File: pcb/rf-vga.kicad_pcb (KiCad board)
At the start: 2 copper layers, 47 parts, among them J1 TEST CONNECTOR, J4 SWD Programming Header, Q1 2N7002, Q2 2N7002, Q3 2N7002, Q4 2N7002, U1 HMC625B, U2 LM1117-3.3, U3 ﻿STM32L010C6

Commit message: PCB updates
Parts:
- added C26: 1u, Capacitor_SMD:C_0603_1608Metric, F.Cu at (189.7, 133.3)
- added C27: 1u, Capacitor_SMD:C_0603_1608Metric, F.Cu at (193.8, 133.3)
- added FB1: GZ2012D601TF, Inductor_SMD:L_0805_2012Metric, F.Cu at (255.0, 97.7)
- added FB2: GZ2012D601TF, Inductor_SMD:L_0805_2012Metric, F.Cu at (255.0, 100.5)
- added J2: Input, parts:SMA_Samtec_SMA-J-P-X-ST-EM1_EdgeMount_withSTEP, F.Cu at (181.6, 77.5)
- added J3: Output, parts:SMA_Samtec_SMA-J-P-X-ST-EM1_EdgeMount_withSTEP, F.Cu at (213.4, 77.5)
- added J5: Conn_01x16_Male, Connector_PinHeader_2.54mm:PinHeader_2x08_P2.54mm_Vertical, B.Cu at (181.6, 114.3)
- added J6: Conn_01x16_Male, Connector_PinHeader_2.54mm:PinHeader_2x08_P2.54mm_Vertical, F.Cu at (210.8, 96.5)
- added J7: Barrel_Jack_Switch, Connector_BarrelJack:BarrelJack_Horizontal, F.Cu at (176.5, 127.0)
- added J8: 30V input, Connector_PinHeader_2.54mm:PinHeader_1x02_P2.54mm_Vertical, F.Cu at (220.9, 119.2)
- added J9: 5V input bypass, Connector_PinHeader_2.54mm:PinHeader_1x02_P2.54mm_Vertical, F.Cu at (167.6, 119.4)
- added R2: 10k, Resistor_SMD:R_0603_1608Metric, F.Cu at (239.1, 101.7)
- added R3: 10k, Resistor_SMD:R_0603_1608Metric, F.Cu at (243.2, 97.6)
- added R4: 10k, Resistor_SMD:R_0603_1608Metric, F.Cu at (239.1, 104.2)
- added R7: 10k, Resistor_SMD:R_0603_1608Metric, F.Cu at (243.1, 101.7)
- added R9: 10k, Resistor_SMD:R_0603_1608Metric, F.Cu at (247.2, 97.6)
- added SW1: Rotary_Encoder_Switch, Rotary_Encoder:RotaryEncoder_Alps_EC11E-Switch_Vertical_H20mm_CircularMountingHoles, F.Cu at (199.4, 124.5)
- added TP1: TestPoint, TestPoint:TestPoint_Pad_2.0x2.0mm, F.Cu at (239.1, 98.4)
- added U4: LM78M05_TO252, Package_TO_SOT_SMD:TO-252-2, F.Cu at (191.8, 127.0)
- C18, C20, C21: value C -> 10n
- moved C17 76.6 mm to (184.6, 132.1), turned to 180 degrees
- moved U2 64.8 mm to (182.9, 126.3), turned to 90 degrees
- moved C19 60.2 mm to (179.1, 122.4), turned to 270 degrees
- moved C21 12.4 mm to (165.6, 72.4)
- moved C6 10.9 mm to (196.6, 73.7)
- moved C7 10.9 mm to (195.1, 73.7)
- moved R1 10.9 mm to (202.7, 84.1)
- moved C1 10.9 mm to (200.4, 74.7)
- moved C11 10.9 mm to (201.9, 87.4)
- moved C13 10.9 mm to (197.4, 84.1)
- moved C16 10.9 mm to (203.5, 78.5)
- moved C2 10.9 mm to (192.8, 80.5)
- moved C5 10.9 mm to (198.1, 73.7)
- moved C8 10.9 mm to (193.5, 73.6)
- moved L1 10.9 mm to (202.7, 81.0)
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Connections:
- C12 pad 1: (no net) -> Net-(C12-Pad1)
- C16 pad 1: (no net) -> Net-(C16-Pad1)
- C18 pad 1: +3V3 -> /mcu/SW
- C18 pad 2: (no net) -> GND
- U1 pad 14: (no net) -> Net-(U1-Pad14)
- U3 pad 1: (no net) -> Net-(U3-Pad1)
- U3 pad 2: (no net) -> Net-(U3-Pad2)
- U3 pad 3: (no net) -> Net-(U3-Pad3)
- U3 pad 38: (no net) -> Net-(U3-Pad38)
- U3 pad 4: (no net) -> Net-(U3-Pad4)
- U3 pad 5: (no net) -> Net-(U3-Pad5)
- U3 pad 6: (no net) -> Net-(U3-Pad6)
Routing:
- net Net-(C26-Pad1): track 0.00 -> 20.4 mm
- net GND: track 8.72 -> 25.0 mm
- net +3V3: track 6.44 -> 17.2 mm
- net +5V: track 0.00 -> 5.06 mm

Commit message: layout check in
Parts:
- removed J6: Conn_01x16_Male, Connector_PinHeader_2.54mm:PinHeader_2x08_P2.54mm_Vertical
- C1, C16: value 1u -> 0.1u; footprint Capacitor_SMD:C_0603_1608Metric -> Capacitor_SMD:C_0402_1005Metric
- C10, C11, C12, C13, C14, C15, C17, C18, C19, C2, C20, C21, C22, C23, C24, C25, C26, C27, C3, C4, C5, C6, C7, C8, C9: footprint Capacitor_SMD:C_0603_1608Metric -> Capacitor_SMD:C_0402_1005Metric
- FB1, FB2: footprint Inductor_SMD:L_0805_2012Metric -> Inductor_SMD:L_0603_1608Metric
- J5: value Conn_01x16_Male -> Conn_02x04_Odd_Even; footprint Connector_PinHeader_2.54mm:PinHeader_2x08_P2.54mm_Vertical -> Connector_PinHeader_2.54mm:PinHeader_2x04_P2.54mm_Vertical
- L1: value 24n -> 3.5u; footprint Inductor_SMD:L_0603_1608Metric -> 4310LC:4310LC
- R1, R10, R12, R14, R15, R16, R17, R18, R2, R3, R4, R5, R6, R7, R8, R9: footprint Resistor_SMD:R_0603_1608Metric -> Resistor_SMD:R_0402_1005Metric
- moved C18 104.3 mm to (215.3, 117.5), turned to 90 degrees
- moved R14 85.5 mm to (200.3, 95.5), turned to 270 degrees
- moved R5 82.0 mm to (206.2, 95.5), turned to 270 degrees
- moved C20 81.7 mm to (200.7, 117.5), turned to 270 degrees
- moved R10 76.1 mm to (190.4, 95.5), turned to 270 degrees
- moved R8 75.6 mm to (204.3, 95.5), turned to 270 degrees
- moved TP1 74.7 mm to (164.5, 97.8)
- moved R16 71.8 mm to (196.4, 95.5), turned to 270 degrees
- moved FB1 68.1 mm to (187.7, 87.1), turned to 180 degrees
- moved FB2 67.9 mm to (187.8, 90.3), turned to 180 degrees
- moved R6 66.8 mm to (198.3, 95.5), turned to 270 degrees
- moved R12 65.3 mm to (202.3, 95.5), turned to 270 degrees
- moved C21 61.2 mm to (207.0, 117.5), turned to 270 degrees
- moved R17 60.9 mm to (188.5, 95.5), turned to 270 degrees
- moved R18 57.9 mm to (194.4, 95.5), turned to 270 degrees
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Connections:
- J5 pad 1: /mcu/ROT_A -> Net-(J5-Pad1)
- J5 pad 2: /mcu/ROT_B -> Net-(J5-Pad2)
- J5 pad 3: /mcu/LE -> Net-(J5-Pad3)
- J5 pad 4: /mcu/SERIAL_CLK -> Net-(J5-Pad4)
- J5 pad 5: /mcu/CONTROL_WORD_BIT -> Net-(J5-Pad5)
- U1 pad 14: Net-(U1-Pad14) -> (no net)
- U1 pad 33: (no net) -> GND
- U3 pad 1: Net-(U3-Pad1) -> (no net)
- U3 pad 15: Net-(J5-Pad6) -> Net-(J5-Pad2)
- U3 pad 16: Net-(J5-Pad7) -> Net-(J5-Pad4)
- U3 pad 17: Net-(J5-Pad8) -> Net-(J5-Pad6)
- U3 pad 2: Net-(U3-Pad2) -> (no net)
- U3 pad 27: Net-(J6-Pad15) -> (no net)
- U3 pad 28: Net-(J6-Pad16) -> (no net)
- U3 pad 29: Net-(J5-Pad9) -> Net-(J5-Pad8)
- U3 pad 3: Net-(U3-Pad3) -> (no net)
- U3 pad 30: Net-(J5-Pad10) -> Net-(J5-Pad7)
- U3 pad 31: Net-(J5-Pad11) -> Net-(J5-Pad5)
- U3 pad 32: Net-(J5-Pad12) -> Net-(J5-Pad3)
- U3 pad 33: Net-(J5-Pad13) -> Net-(J5-Pad1)
- U3 pad 38: Net-(U3-Pad38) -> (no net)
- U3 pad 4: Net-(U3-Pad4) -> (no net)
- U3 pad 5: Net-(U3-Pad5) -> (no net)
- U3 pad 6: Net-(U3-Pad6) -> (no net)
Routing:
- net +5V: track 5.06 -> 62.8 mm, vias 0 -> 2
- net /mcu/LE: track 0.00 -> 52.9 mm, vias 0 -> 2
- net /mcu/CONTROL_WORD_BIT: track 0.00 -> 48.8 mm, vias 0 -> 2
- net /mcu/SERIAL_CLK: track 0.00 -> 47.8 mm, vias 0 -> 2
- net /mcu/SEG_DOT: track 0.00 -> 46.7 mm, vias 0 -> 2
- net /mcu/SEG_E: track 0.00 -> 43.3 mm, vias 0 -> 4
- net /mcu/SEG_COLON: track 0.00 -> 43.1 mm, vias 0 -> 4
- net /mcu/SEG_A: track 0.00 -> 38.8 mm, vias 0 -> 4
- net /mcu/SEG_DP: track 0.00 -> 38.7 mm, vias 0 -> 2
- net /mcu/SEG_C: track 0.00 -> 37.4 mm, vias 0 -> 4
- net /mcu/SEG_F: track 0.00 -> 35.5 mm, vias 0 -> 2
- net +3V3: track 17.2 -> 52.5 mm
- net /mcu/DIG4: track 0.00 -> 35.1 mm, vias 0 -> 2
- net /mcu/SEG_B: track 0.00 -> 33.1 mm, vias 0 -> 2
- net /mcu/DIG3: track 0.00 -> 30.5 mm, vias 0 -> 4
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- added copper zone on F.Cu, net GND

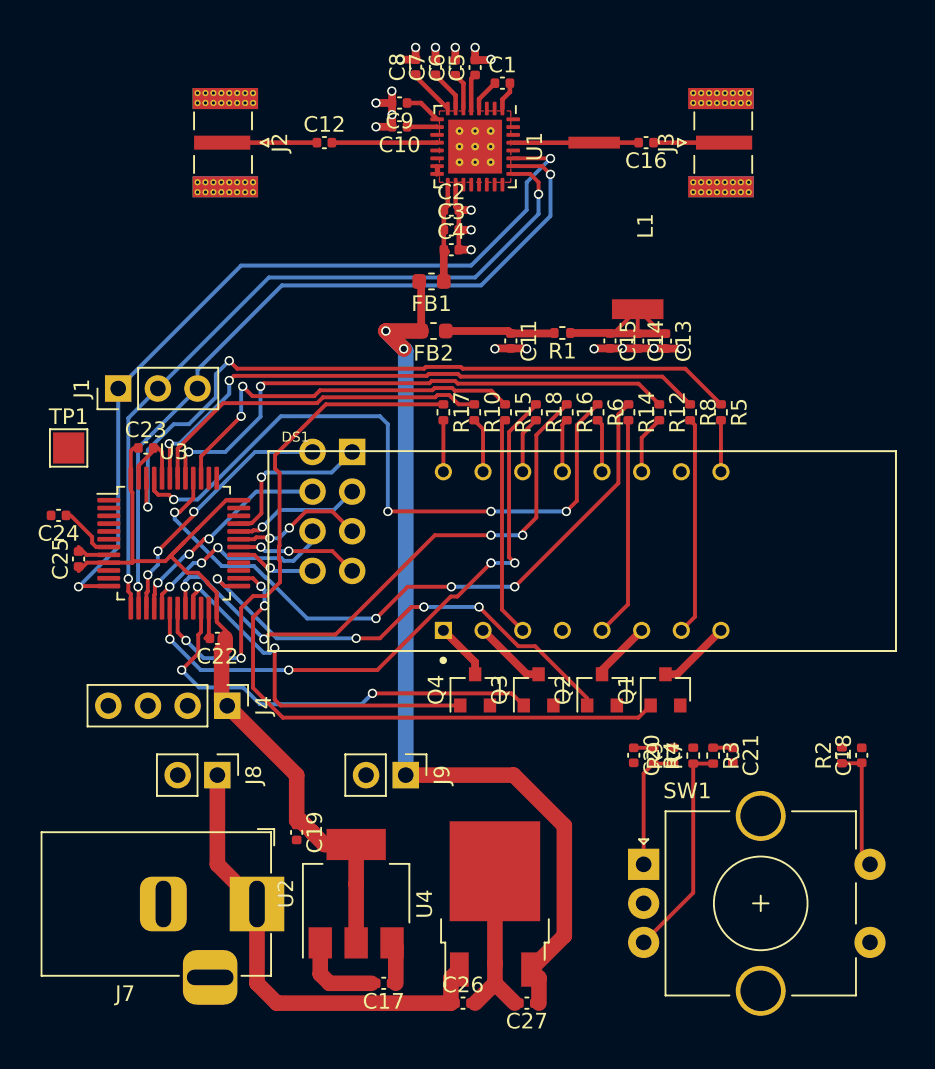
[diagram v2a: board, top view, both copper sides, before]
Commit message: Completed PCB layout
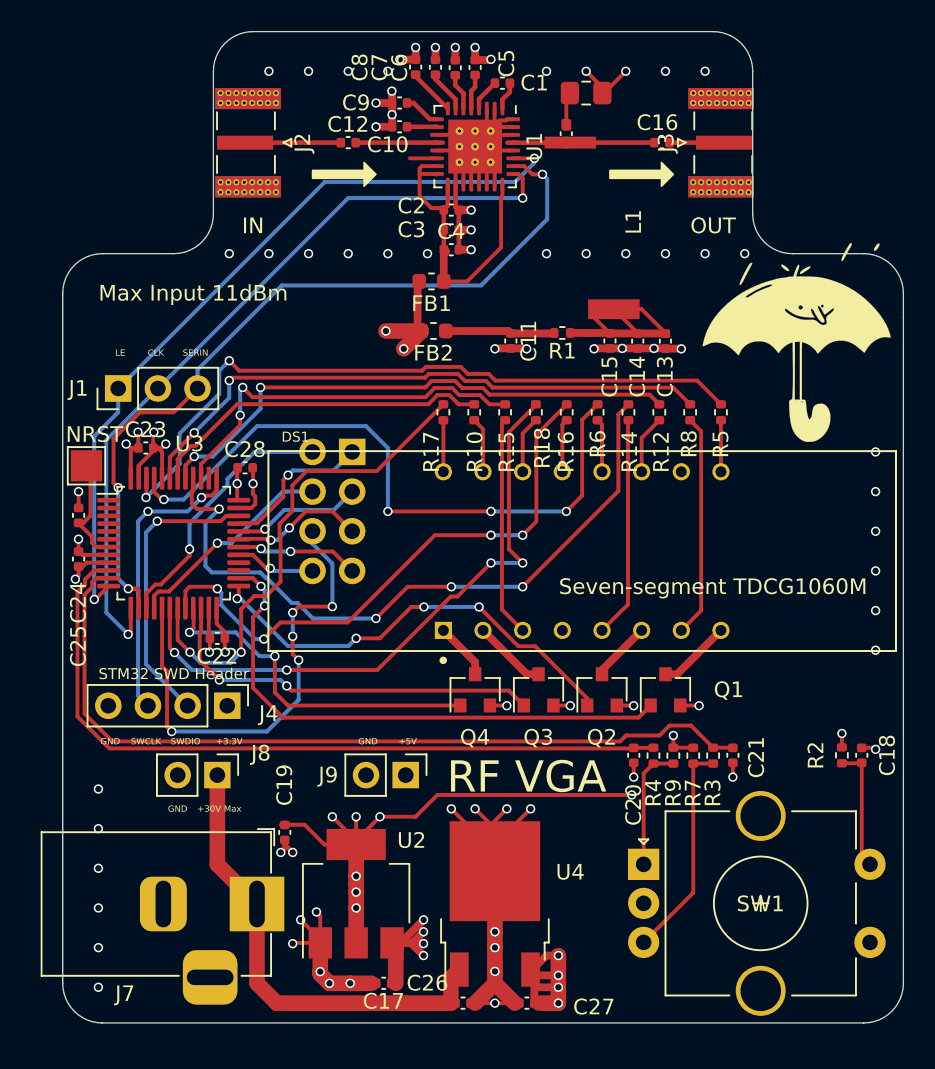
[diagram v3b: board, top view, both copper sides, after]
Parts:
- removed TP1: TestPoint, TestPoint:TestPoint_Pad_2.0x2.0mm
- added C28: 100n, Capacitor_SMD:C_0402_1005Metric, F.Cu at (175.8, 99.1)
- added G***: LOGO, parts:text, B.Cu at (194.8, 105.7)
- added G***: LOGO, parts:umbrella, F.Cu at (211.3, 90.9)
- added NRST: TestPoint, TestPoint:TestPoint_Pad_2.0x2.0mm, F.Cu at (165.6, 98.9)
- added REF**: C_0805_2012Metric_Pad1.18x1.45mm_HandSolder, Capacitor_SMD:C_0805_2012Metric_Pad1.18x1.45mm_HandSolder, F.Cu at (197.6, 75.1)
- added REF**: L_0402_1005Metric_Pad0.77x0.64mm_HandSolder, Inductor_SMD:L_0402_1005Metric_Pad0.77x0.64mm_HandSolder, F.Cu at (196.3, 77.7)
- C12: value 1u -> 0.1u
- DS1: value TDCG1060M -> Seven-segment TDCG1060M
- moved C12 1.52 mm to (182.4, 78.2)
- moved L1 1.52 mm to (199.4, 83.6)
- moved J2 1.47 mm to (176.0, 78.2)
- moved C24 1.28 mm to (165.1, 102.1), turned to 90 degrees
- moved C16 1.02 mm to (202.5, 78.2)
- moved C19 0.76 mm to (178.3, 122.4)
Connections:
- net Net-(C13-Pad1) renamed /vga/V_BIAS
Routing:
- net GND: track 48.9 -> 115.3 mm, vias 19 -> 81
- net /mcu/ROT_B: track 1.27 -> 53.1 mm
- net /mcu/ROT_A: track 1.27 -> 48.5 mm
- net /mcu/SWCLK: track 0.00 -> 18.7 mm, vias 0 -> 2
- net /mcu/SWDIO: track 0.00 -> 18.6 mm, vias 0 -> 1
- net Net-(J5-Pad6): track 13.3 -> 30.9 mm, vias 3 -> 5
- net +5VL: track 6.96 -> 21.1 mm
- net +3V3: track 52.5 -> 65.3 mm, vias 0 -> 14
- net +5V: track 62.8 -> 58.8 mm, vias 2 -> 10
- net (no net): track 0.00 -> 3.88 mm
- net /mcu/~RST: track 3.52 -> 6.95 mm
- net /mcu/LE: track 52.9 -> 49.7 mm
- net /mcu/CONTROL_WORD_BIT: track 48.8 -> 51.9 mm, vias 2 -> 3
- net /mcu/DIG2: track 27.9 -> 25.3 mm
- net /mcu/DIG3: track 30.5 -> 28.4 mm
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- added copper zone on In2.Cu, net +3V3
- added copper zone on In2.Cu, net +5V
- added copper zone on In1.Cu, net GND
- added copper zone on In2.Cu, net GND
- removed copper zone on F.Cu, net GND
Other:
- board outline added: 53.8 x 63.5 mm
- copper layers 2 -> 4
- board text added: "+3.3V"
- board text added: "+30V Max"
- board text added: "+5V"
- board text added: "CLK"
- board text added: "GND"
- board text added: "IN"
- board text added: "LE"
- board text added: "Max Input 11dBm"
- board text added: "OUT"
- board text added: "RF VGA"
- board text added: "SERIN"
- board text added: "STM32 SWD Header"
- board text added: "SWCLK"
- board text added: "SWDIO"

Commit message: final tweaks and produce outputs for jlcpcb fabrication
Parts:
- C22, C23, C25, C28: value 100n -> 0.1u
- DS1: value Seven-segment TDCG1060M -> TDCG1060M
- FB1, FB2: footprint Inductor_SMD:L_0603_1608Metric -> Inductor_SMD:L_0805_2012Metric
- R1: footprint Resistor_SMD:R_0402_1005Metric -> Resistor_SMD:R_0805_2012Metric_Pad1.20x1.40mm_HandSolder
- moved R1 0.55 mm to (195.7, 90.9)
- moved REF** 0.08 mm to (196.4, 77.7)
- renumbered NRST to TP1
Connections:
- U1 pad 14: (no net) -> Net-(U1-Pad14)
- U3 pad 1: (no net) -> +3V3
- U3 pad 2: (no net) -> Net-(U3-Pad2)
- U3 pad 27: (no net) -> Net-(U3-Pad27)
- U3 pad 28: (no net) -> Net-(U3-Pad28)
- U3 pad 3: (no net) -> Net-(U3-Pad3)
- U3 pad 38: (no net) -> Net-(U3-Pad38)
- U3 pad 4: (no net) -> Net-(U3-Pad4)
- U3 pad 5: (no net) -> Net-(U3-Pad5)
- U3 pad 6: (no net) -> Net-(U3-Pad6)
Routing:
- net +3V3: track 65.3 -> 68.8 mm, vias 14 -> 15
- net Net-(U1-Pad14): track 0.00 -> 1.74 mm
- net (no net): track 3.88 -> 2.29 mm
